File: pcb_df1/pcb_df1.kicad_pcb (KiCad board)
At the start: 2 copper layers, 4 parts, among them Q1 DMG2301L, Q2 BSS123

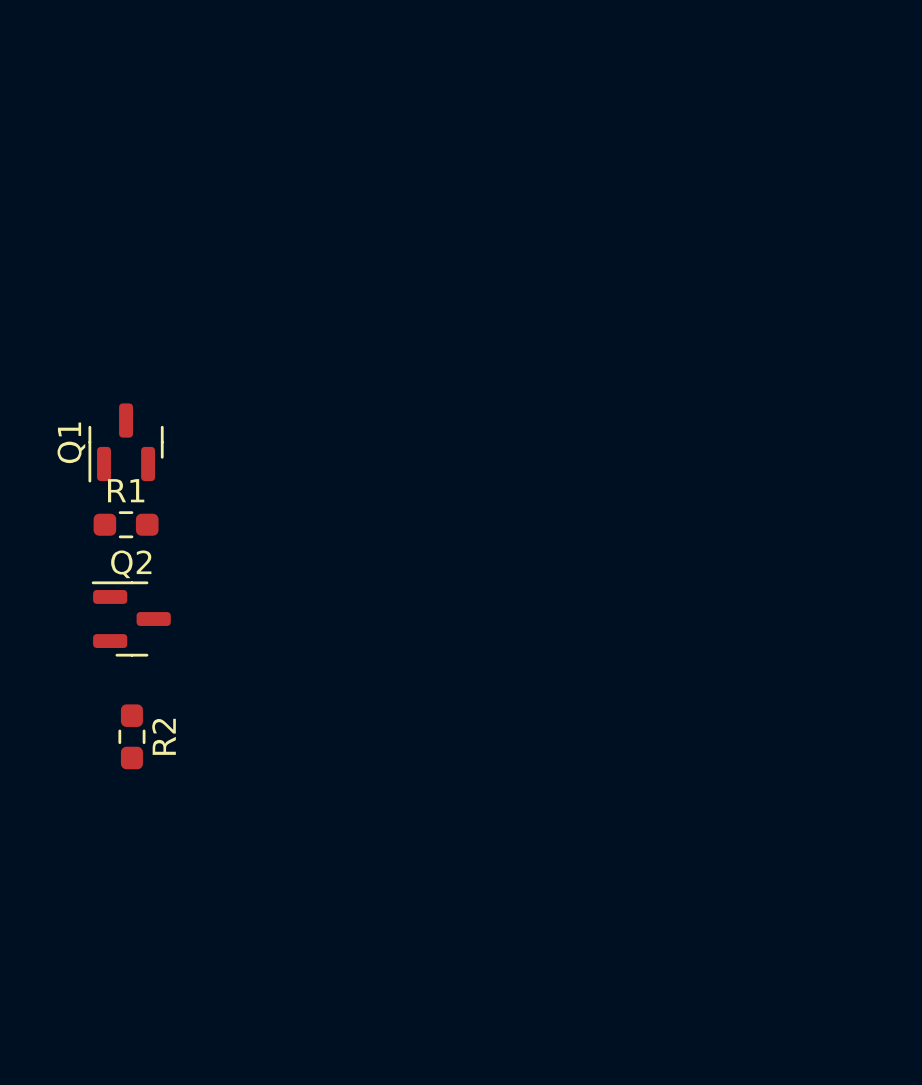
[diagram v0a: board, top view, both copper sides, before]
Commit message: DF1 (floppy detection) PCB completed.
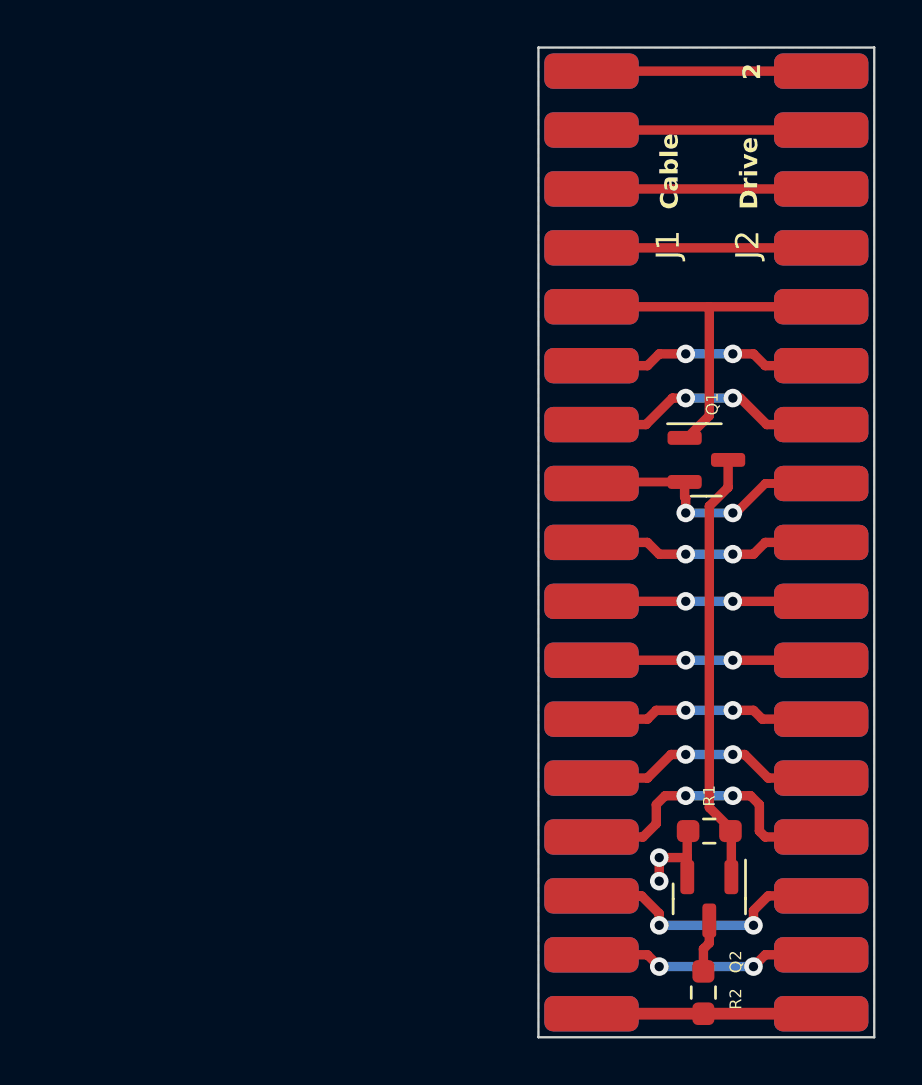
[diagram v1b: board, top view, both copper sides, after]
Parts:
- added J1: Cable, pcb_df1:idc34_edge, B.Cu at (119.6, 59.7)
- added J2: Floppy, pcb_df1:idc34_edge, B.Cu at (129.5, 59.7)
- moved R1 28.4 mm to (124.7, 92.5), turned to 180 degrees
- moved Q2 27.7 mm to (124.7, 95.4), turned to -90 degrees
- moved R2 27.0 mm to (124.5, 99.4)
- moved Q1 25.0 mm to (124.6, 76.5), turned to 0 degrees
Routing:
- net Net-(Q1-D): track 0.00 -> 18.7 mm
- net /~{SEL0}: track 0.00 -> 16.3 mm
- net Net-(J1-Pin_28): track 0.00 -> 12.5 mm, vias 0 -> 2
- net /~{MTRON}: track 0.00 -> 12.0 mm, vias 0 -> 2
- net Net-(J1-Pin_30): track 0.00 -> 11.6 mm, vias 0 -> 2
- net Net-(J1-Pin_14): track 0.00 -> 10.9 mm, vias 0 -> 2
- net Net-(J1-Pin_26): track 0.00 -> 10.5 mm, vias 0 -> 2
- net Net-(J1-Pin_18): track 0.00 -> 10.3 mm, vias 0 -> 2
- net Net-(J1-Pin_12): track 0.00 -> 10.3 mm, vias 0 -> 2
- net Net-(J1-Pin_32): track 0.00 -> 10.1 mm, vias 0 -> 2
- net Net-(J1-Pin_24): track 0.00 -> 9.97 mm, vias 0 -> 2
- net Net-(J1-Pin_8): track 0.00 -> 9.91 mm
- net Net-(J1-Pin_6): track 0.00 -> 9.91 mm
- net Net-(J1-Pin_4): track 0.00 -> 9.91 mm
- net Net-(J1-Pin_2): track 0.00 -> 9.91 mm
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- added copper zone on B.Cu, net GND
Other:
- board outline added: 14.5 x 42.7 mm
- board text added: "1"
- board text added: "2"
- board text added: "33"
- board text added: "Cable"
- board text added: "Drive"
- board text added: "YAFS v1.0"
